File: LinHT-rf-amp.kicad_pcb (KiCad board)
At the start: 4 copper layers, 35 x 20 mm, 26 parts, among them J1 SIGNALS, J2 INPUT, J3 OUTPUT, U1 GRF5604

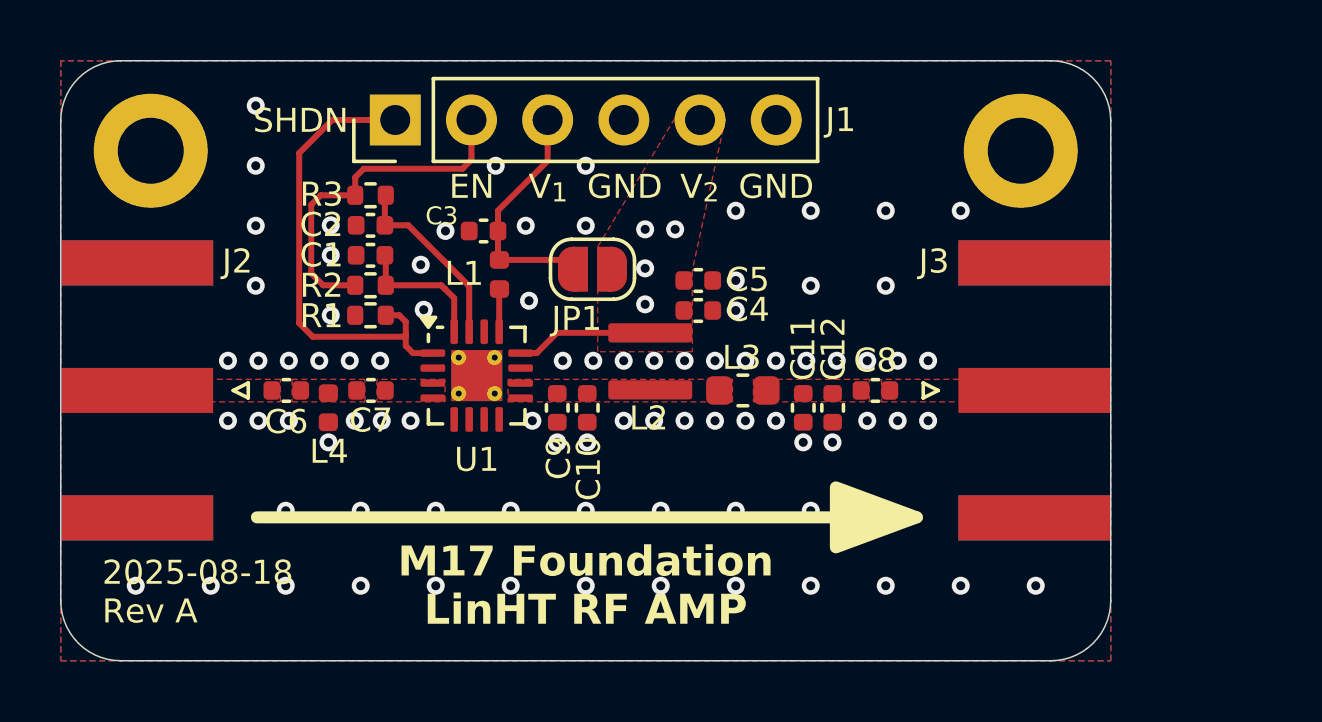
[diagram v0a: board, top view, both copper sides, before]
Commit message: Updated layout with the low pass filter
Board dimensions has to be increased to 40x20 mm (original 35x20mm)
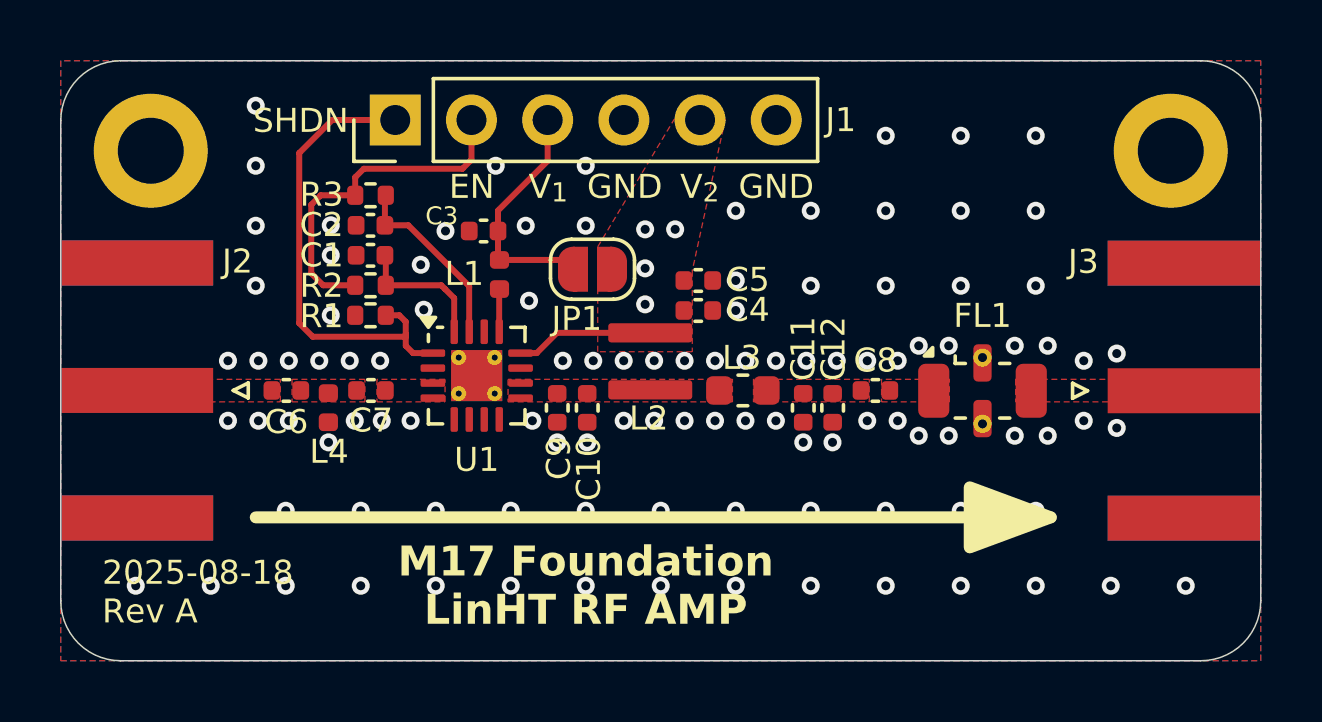
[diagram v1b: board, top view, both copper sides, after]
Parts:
- added FL1: LFCN-490, Filter:Filter_Mini-Circuits_FV1206, F.Cu at (165.1, 96.9)
- moved H2 5.00 mm to (171.3, 88.9)
- moved J3 4.98 mm to (171.8, 96.9)
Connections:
- C8 pad 2: Net-(J3-In) -> Net-(FL1-IN)
- J3 pad 1: Net-(J3-In) -> Net-(FL1-OUT)
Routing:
- net GND: vias 85 -> 105
- added copper zone on F.Cu, net Net-(FL1-IN)
- added copper zone on F.Cu, net Net-(FL1-OUT)
- removed copper zone on F.Cu, net Net-(J3-In)
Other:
- board size 35 x 20 mm -> 40 x 20 mm

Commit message: Updated  design to use new GRF5604 footprint
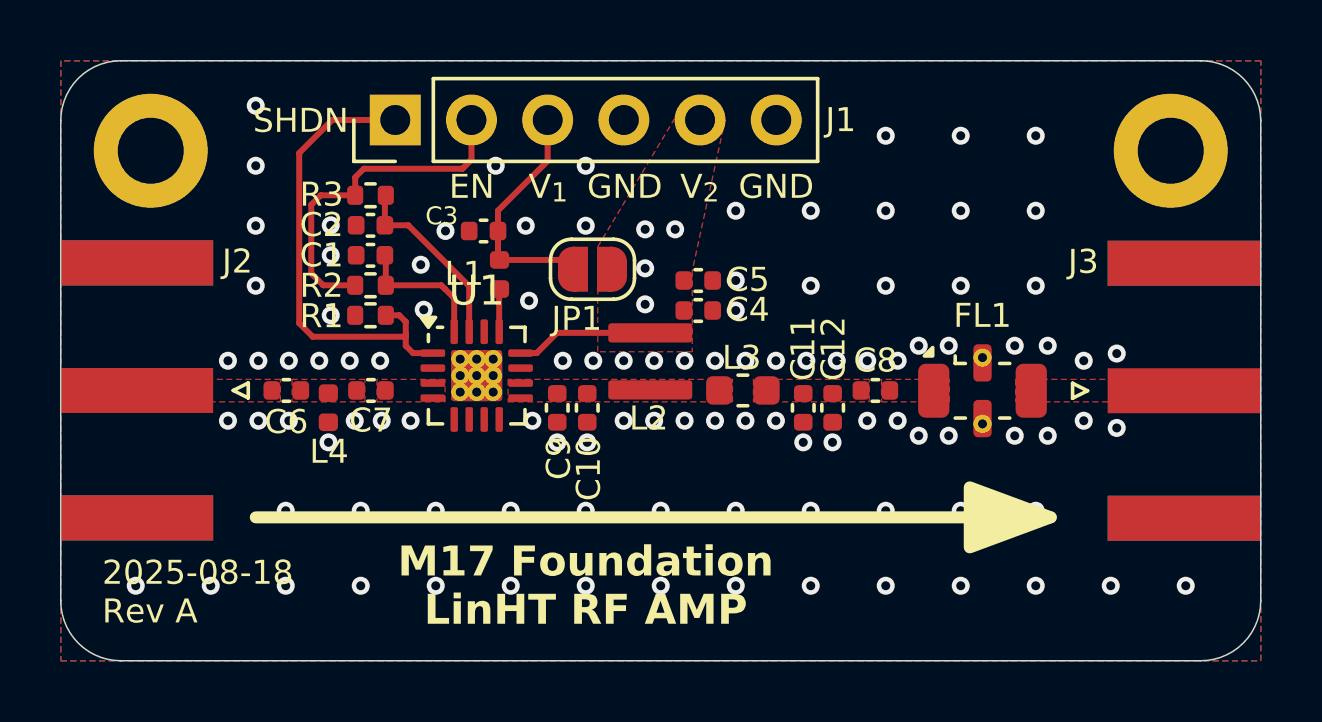
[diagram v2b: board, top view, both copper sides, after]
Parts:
- U1: footprint Package_DFN_QFN:QFN-16-1EP_3x3mm_P0.5mm_EP1.7x1.7mm_ThermalVias -> Parts:QFN-16-1EP_3x3mm_P0.5mm_EP1.7x1.7mm_ThermalVias
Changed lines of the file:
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@@
 		(embedded_fonts no)
 	)
-	(footprint "Package_DFN_QFN:QFN-16-1EP_3x3mm_P0.5mm_EP1.7x1.7mm_ThermalVias"
+	(footprint "Parts:QFN-16-1EP_3x3mm_P0.5mm_EP1.7x1.7mm_ThermalVias"
 		(layer "F.Cu")
 		(at 148.215 96.37)
@@
 		(tags "QFN NoLead")
 		(property "Reference" "U1"
-			(at 0 2.805 0)
+			(at 0 -2.83 0)
 			(layer "F.SilkS")
 			(effects
 				(font
-					(size 0.8 0.8)
+					(size 1 1)
 					(thickness 0.15)
 				)
@@
 			(effects
 				(font
-					(size 0.8 0.8)
+					(size 0.75 0.75)
 					(thickness 0.11)
 				)
@@
 		)
 		(pad "17" thru_hole circle
-			(at -0.6 -0.6)
-			(size 0.5 0.5)
-			(drill 0.2)
-			(property pad_prop_heatsink)
-			(layers "*.Cu")
-			(remove_unused_layers no)
-			(net 1 "GND")
-			(pinfunction "GND")
-			(pintype "power_in")
-		)
-		(pad "17" thru_hole circle
-			(at -0.6 0.6)
-			(size 0.5 0.5)
-			(drill 0.2)
-			(property pad_prop_heatsink)
-			(layers "*.Cu")
-			(remove_unused_layers no)
-			(net 1 "GND")
-			(pinfunction "GND")
-			(pintype "power_in")
-		)
-		(pad "17" smd rect
+			(at -0.55 -0.55)
+			(size 0.6 0.6)
+			(drill 0.3)
+			(property pad_prop_heatsink)
+			(layers "*.Cu")
+			(remove_unused_layers no)
+			(net 1 "GND")
+			(pinfunction "GND")
+			(pintype "power_in")
+		)
+		(pad "17" thru_hole circle
+			(at -0.55 0)
+			(size 0.6 0.6)
+			(drill 0.3)
+			(property pad_prop_heatsink)
+			(layers "*.Cu")
+			(remove_unused_layers no)
+			(net 1 "GND")
+			(pinfunction "GND")
+			(pintype "power_in")
+		)
+		(pad "17" thru_hole circle
+			(at -0.55 0.55)
+			(size 0.6 0.6)
+			(drill 0.3)
+			(property pad_prop_heatsink)
+			(layers "*.Cu")
+			(remove_unused_layers no)
+			(net 1 "GND")
+			(pinfunction "GND")
+			(pintype "power_in")
+		)
+		(pad "17" thru_hole circle
+			(at 0 -0.55)
+			(size 0.6 0.6)
+			(drill 0.3)
+			(property pad_prop_heatsink)
+			(layers "*.Cu")
+			(remove_unused_layers no)
+			(net 1 "GND")
+			(pinfunction "GND")
+			(pintype "power_in")
+		)
+		(pad "17" thru_hole circle
+			(at 0 0)
+			(size 0.6 0.6)
+			(drill 0.3)
+			(property pad_prop_heatsink)
+			(layers "*.Cu")
+			(remove_unused_layers no)
+			(net 1 "GND")
+			(pinfunction "GND")
+			(pintype "power_in")
+		)
+		(pad "17" smd roundrect
 			(at 0 0)
 			(size 1.7 1.7)
 			(property pad_prop_heatsink)
 			(layers "F.Cu" "F.Mask")
+			(roundrect_rratio 0.05882352941)
 			(net 1 "GND")
 			(pinfunction "GND")
@@
 			(zone_connect 2)
 		)
-		(pad "17" smd rect
+		(pad "17" smd roundrect
 			(at 0 0)
 			(size 1.7 1.7)
 			(property pad_prop_heatsink)
 			(layers "B.Cu")
+			(roundrect_rratio 0.05882352941)
 			(net 1 "GND")
 			(pinfunction "GND")
@@
 		)
 		(pad "17" thru_hole circle
-			(at 0.6 -0.6)
-			(size 0.5 0.5)
-			(drill 0.2)
-			(property pad_prop_heatsink)
-			(layers "*.Cu")
-			(remove_unused_layers no)
-			(net 1 "GND")
-			(pinfunction "GND")
-			(pintype "power_in")
-		)
-		(pad "17" thru_hole circle
-			(at 0.6 0.6)
-			(size 0.5 0.5)
-			(drill 0.2)
-			(property pad_prop_heatsink)
-			(layers "*.Cu")
+			(at 0 0.55)
+			(size 0.6 0.6)
+			(drill 0.3)
+			(property pad_prop_heatsink)
+			(layers "*.Cu")
+			(remove_unused_layers no)
+			(net 1 "GND")
+			(pinfunction "GND")
+			(pintype "power_in")
+		)
+		(pad "17" thru_hole circle
+			(at 0.55 -0.55)
+			(size 0.6 0.6)
+			(drill 0.3)
+			(property pad_prop_heatsink)
+			(layers "*.Cu")
+			(remove_unused_layers no)
+			(net 1 "GND")
+			(pinfunction "GND")
+			(pintype "power_in")
+		)
+		(pad "17" thru_hole circle
+			(at 0.55 0)
+			(size 0.6 0.6)
+			(drill 0.3)
+			(property pad_prop_heatsink)
+			(layers "*.Cu")
+			(remove_unused_layers no)
+			(net 1 "GND")
+			(pinfunction "GND")
+			(pintype "power_in")
+		)
+		(pad "17" thru_hole circle
+			(at 0.55 0.55)
+			(size 0.6 0.6)
+			(drill 0.3)
+			(property pad_prop_heatsink)
+			(layers "*.Cu")
